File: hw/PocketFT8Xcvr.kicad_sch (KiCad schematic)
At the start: 55 parts, among them J1 HX8357D, J2 ANT, J3 +12V, J4 Conn_01x07, Q1 2N3904, Q2 2N3906, Q3 2N7000, Q4 2N7000, U1 MCP3422, U2 Si4735-D60-GU, U3 GVA-84, U4 L7805CV

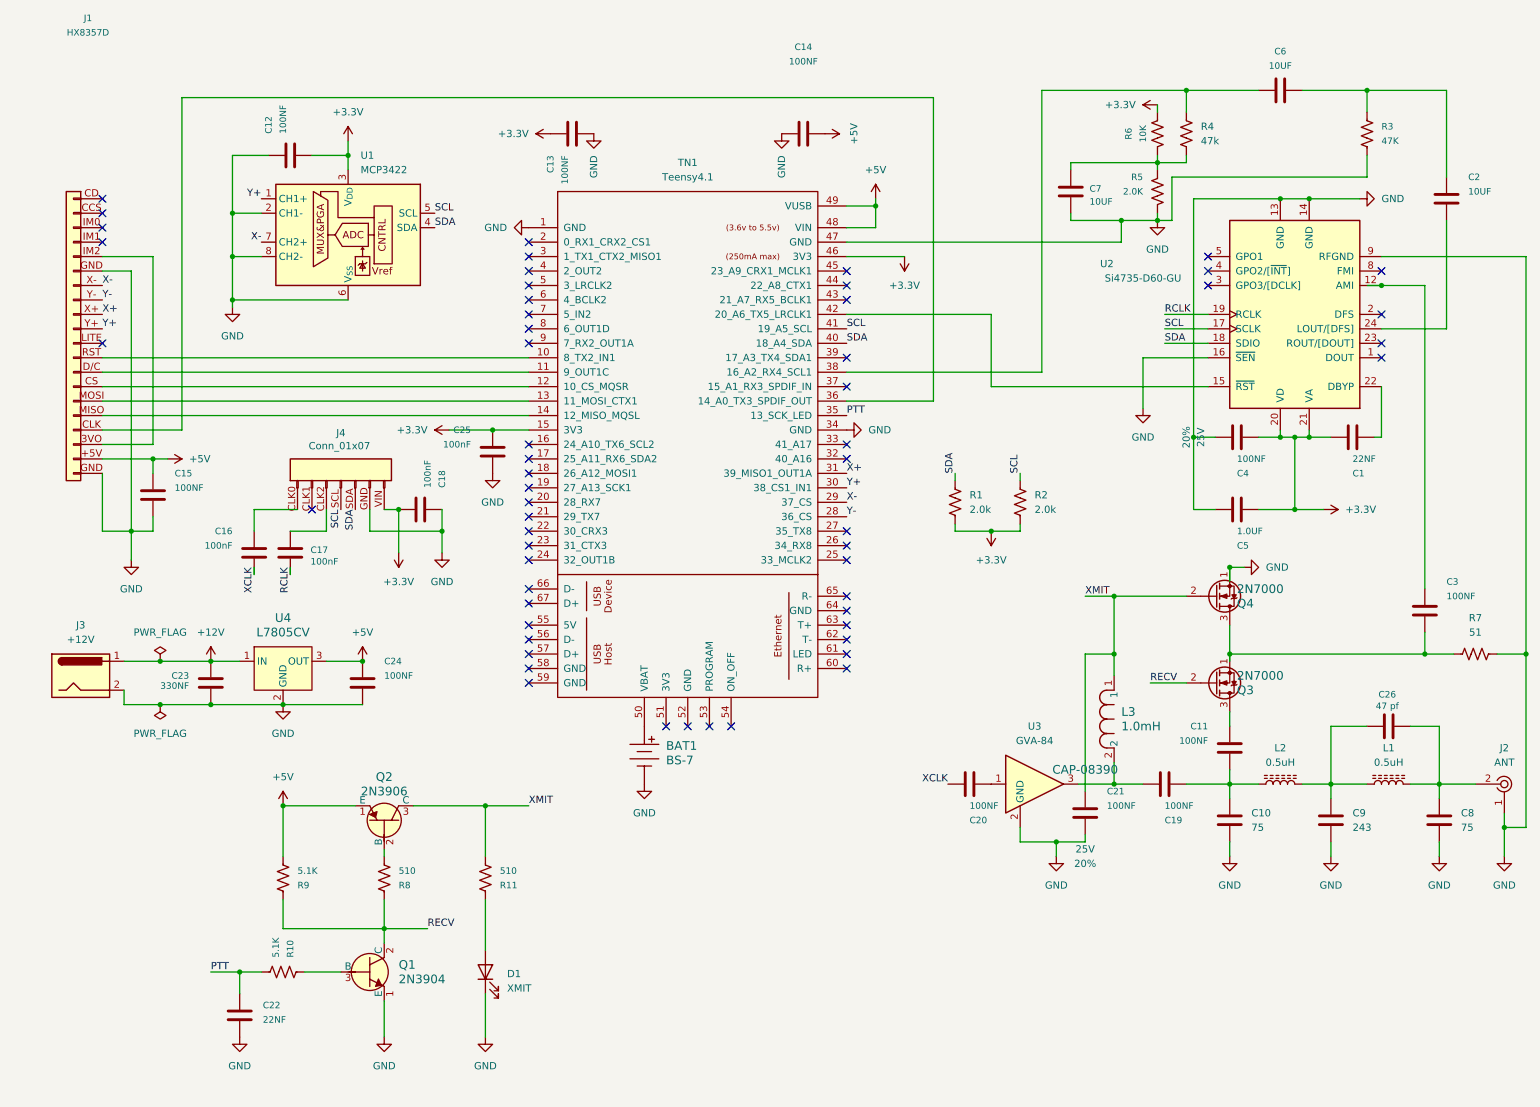
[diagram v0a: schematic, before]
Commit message: BOM construction begun
Connectors and capacitors
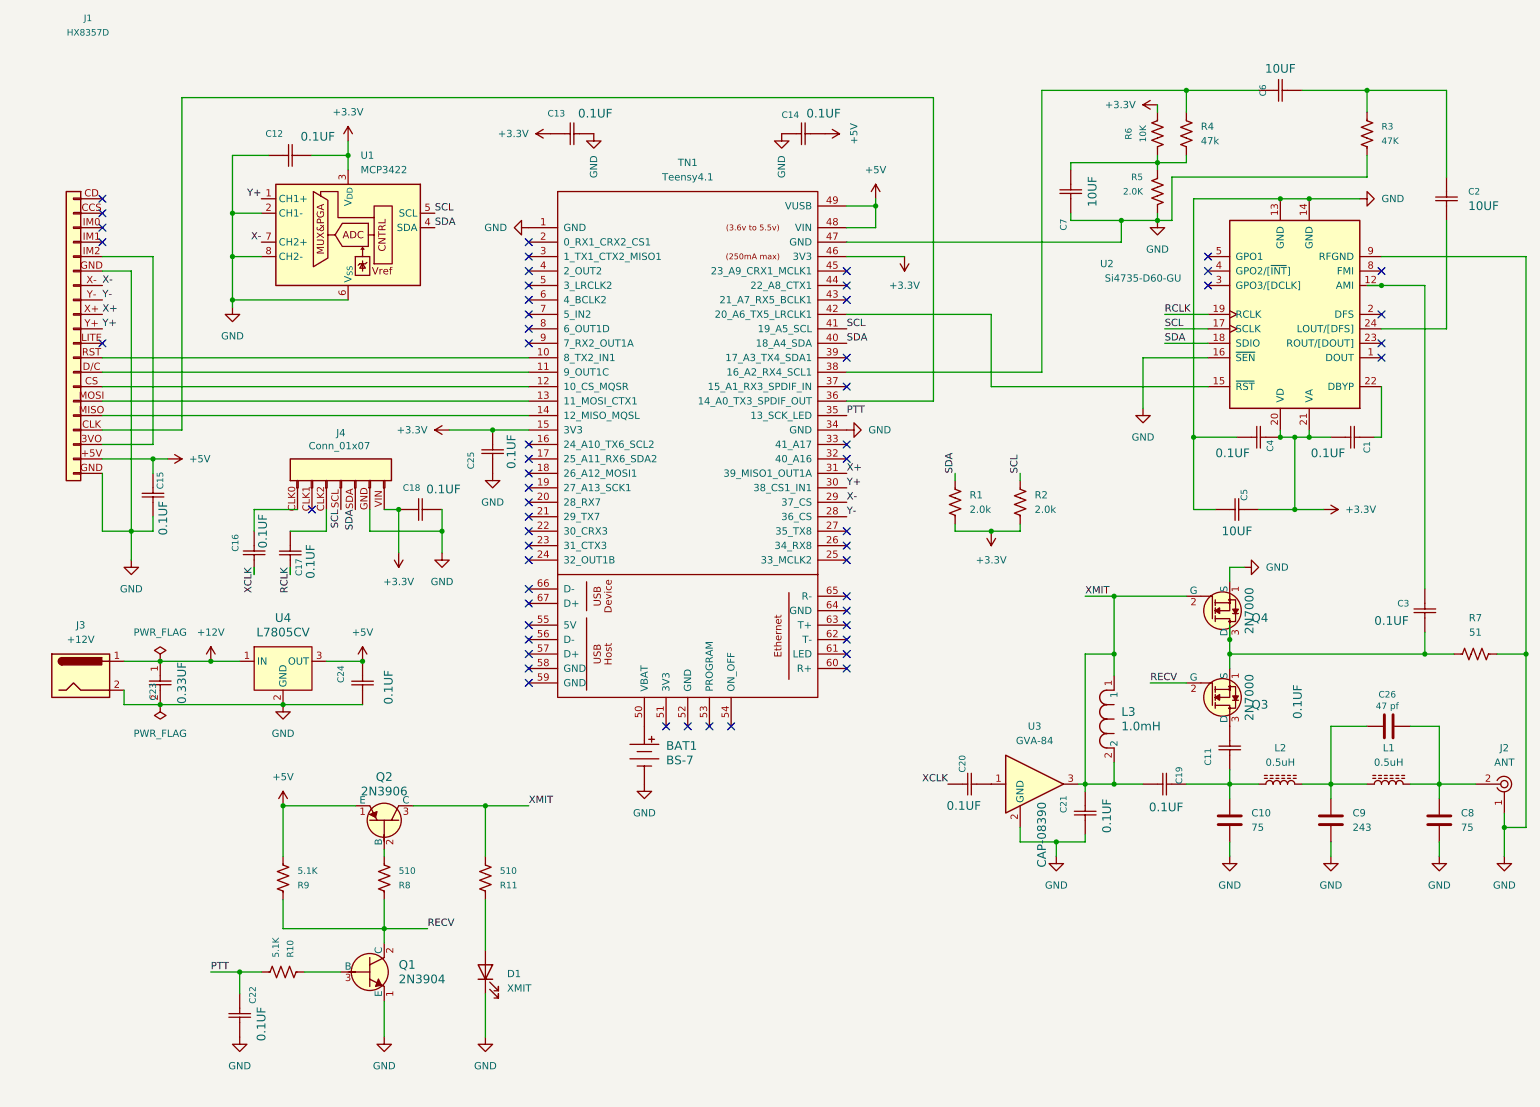
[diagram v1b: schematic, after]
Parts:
- C1, C22: value 22NF -> 0.1UF; footprint SparkFun-Capacitor:C_0603_1608Metric -> 0603; symbol SparkFun-Capacitor:0.1uF_0603_25V_20% -> Kemet2024-08-02_22-05-35:C0603C104K4RACTU; Manufacturer (none) -> Kemet; Mfg Part # (none) -> C0603C104K4RAC7867; Tolerance 20% -> 10%; Voltage 25V -> 16V
- C11, C12, C13, C14, C15, C19, C20, C21, C24, C3, C4: value 100NF -> 0.1UF; footprint SparkFun-Capacitor:C_0603_1608Metric -> 0603; symbol SparkFun-Capacitor:0.1uF_0603_25V_20% -> Kemet2024-08-02_22-05-35:C0603C104K4RACTU; Manufacturer (none) -> Kemet; Mfg Part # (none) -> C0603C104K4RAC7867; Tolerance 20% -> 10%; Voltage 25V -> 16V
- C16, C17, C18, C25: value 100nF -> 0.1UF; footprint SparkFun-Capacitor:C_0603_1608Metric -> 0603; symbol SparkFun-Capacitor:0.1uF_0603_25V_20% -> Kemet2024-08-02_22-05-35:C0603C104K4RACTU; Manufacturer (none) -> Kemet; Mfg Part # (none) -> C0603C104K4RAC7867; Tolerance 20% -> 10%; Voltage 25V -> 16V
- C2, C6, C7: footprint SparkFun-Capacitor:C_0603_1608Metric -> 0805; symbol SparkFun-Capacitor:10uF_0603_6.3V_20% -> Kemet2024-08-02_22-55-33:C0805C334K4RAC7800; Manufacturer (none) -> Kemet; Mfg Part # (none) -> C0805C106K4PAC7800
- C23: value 330NF -> 0.33UF; footprint 0603 -> 0805; symbol Device:C -> Kemet2024-08-02_22-55-33:C0805C334K4RAC7800; Manufacturer (none) -> Kemet; Mfg Part # (none) -> C0805C334K4RAC7800
- C5: value 1.0UF -> 10UF; footprint SparkFun-Capacitor:C_0603_1608Metric -> 0805; symbol SparkFun-Capacitor:1.0uF_0603_16V_10% -> Kemet2024-08-02_22-55-33:C0805C334K4RAC7800; Manufacturer (none) -> Kemet; Mfg Part # (none) -> C0805C106K4PAC7800
- Q3, Q4: footprint Package_TO_SOT_THT:TO-92_Inline -> digikey-footprints:TO-92-3; symbol Transistor_FET:2N7000 -> dk_Transistors-FETs-MOSFETs-Single:2N7000; Category (none) -> Discrete Semiconductor Products; DK_Datasheet_Link (none) -> https://www.onsemi.com/pub/Collateral/NDS7002A-D.PDF; DK_Detail_Page (none) -> /product-detail/en/on-semiconductor/2N7000/2N7000FS-ND/2442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; Description_1 (none) -> MOSFET N-CH 60V 200MA TO-92; Digi-Key_PN (none) -> 2N7000FS-ND; Family (none) -> Transistors - FETs, MOSFETs - Single; MPN (none) -> 2N7000; Manufacturer (none) -> ON Semiconductor; Status (none) -> Active
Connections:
- net +3.3V: now also C1.1, C12.1, C4.2, C5.2; no longer C1.2, C12.2, C4.1, C5.1
- net +5V: now also C14.2, C15.2, C24.2; no longer C14.1, C15.1, C24.1
- net GND: now also C12.2, C14.1, C15.1, C21.1, C22.1, C24.1, C4.1, C5.1, C7.1; no longer C12.1, C14.2, C15.2, C21.2, C22.2, C24.2, C4.2, C5.2, C7.2
- net PTT: now also C22.2; no longer C22.1
- net RCLK: now also C17.1; no longer C17.2
- net XCLK: now also C20.1; no longer C20.2
- net XMIT: now also C19.1, C21.2, L3.2, U3.3; no longer C21.1
- net at R4.1, R5.2, R6.1: now also C7.2; no longer C7.1
- net at Q3.1 (S), Q4.3 (D), R7.2: now also C3.1; no longer C3.2
- net at C10.1, C11.2, L2.1: now also C19.2; no longer C19.1
- net at U2.22 (DBYP): now also C1.2; no longer C1.1
- net at R4.2, TN1.38 (16_A2_RX4_SCL1): now also C6.2; no longer C6.1
- net at C2.2: now also C6.1, R3.2; no longer U2.24 (LOUT/[DFS])
- net at U3.1: now also C20.2; no longer C20.1
- net at U2.12 (AMI): now also C3.2; no longer C3.1
- net at J4.CLK2: now also C17.2; no longer C17.1
- new net: C2.1, U2.24 (LOUT/[DFS])

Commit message: Ongoing construction of BOM
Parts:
- removed R8: 510, SparkFun-Resistor:R_0603_1608Metric, symbol SparkFun-Resistor:2.0k_0603
- added R8: 510, 0603, symbol Device:R_US
- C1, C11, C12, C13, C14, C15, C16, C17, C18, C19, C2, C20, C21, C22, C23, C24, C25, C3, C4, C5, C6, C7: Notes (none) -> Substitutions OK
- C10, C8: value 75 -> 75PF; now not fitted; now left out of the parts list
- C26: value 47 pf -> 47PF; footprint Capacitor_SMD:C_0805_2012Metric -> 0805; now not fitted; now left out of the parts list
- C9: value 243 -> 243PF; now not fitted; now left out of the parts list
- L1, L2: now not fitted; now left out of the parts list
- L3: Manufacturer (none) -> Bourns; Mfg Part # (none) -> RLB9012-102KL
- Q3: Mfg Part # (none) -> 2N7000
- Q4: Mfg Part # (none) -> 2N7000; Notes (none) -> Substitions OK; Status Active -> (none)
- R1: value 2.0k -> 2.0K; footprint SparkFun-Resistor:R_0603_1608Metric -> 0603; Manufacturer (none) -> Yageo; Mfg Part # (none) -> RC0603JR-072KL; Notes (none) -> Substitutions OK; PROD_ID RES-08296 -> (none)
- R10, R9: footprint SparkFun-Resistor:R_0603_1608Metric -> 0603; Manufacturer (none) -> Yageo; Mfg Part # (none) -> RC0603JR-075K1L; Notes (none) -> Substitutions OK; PROD_ID RES-12083 -> (none)
- R11: footprint SparkFun-Resistor:R_0603_1608Metric -> 0603; symbol SparkFun-Resistor:2.0k_0603 -> Device:R_US; Manufacturer (none) -> Yageo; Mfg Part # (none) -> RC0603JR-07510RL; Notes (none) -> Substitutions OK
- R2: footprint SparkFun-Resistor:R_0603_1608Metric -> 0603; Manufacturer (none) -> Yageo; Mfg Part # (none) -> RC0603JR-072KL; Notes (none) -> Substitutions OK
- R3, R4: footprint SparkFun-Resistor:R_0603_1608Metric -> 0603; Manufacturer (none) -> Yageo; Mfg Part # (none) -> RC0603JR-0747KL; Notes (none) -> Substitutions OK
- R6: footprint SparkFun-Resistor:R_0603_1608Metric -> 0603; Manufacturer (none) -> YAGEO; Mfg Part # (none) -> RC0603JR-0710KL; Notes (none) -> Substitutions OK
- R7: value 51 -> 51 OHM
- U4: MPN L7805CV -> (none); Mfg Part # (none) -> L7805CV
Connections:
- net RECV: now also R8.2
- net XMIT: now also R11.1; no longer R11.2
- net at Q2.2 (B): now also R8.1
- net at D1.2 (A): now also R11.2; no longer R11.1
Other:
- moved on the sheet: R11, R9

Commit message: Ongoing BOM construction
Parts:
- BAT1: MPN BS-7 -> (none); Mfg Part # (none) -> BS-7; Type (none) -> SMD
- C1, C11, C12, C13, C14, C15, C16, C17, C18, C19, C2, C20, C21, C22, C23, C24, C25, C3, C4, C5, C6, C7, R1, R10, R3, R6, R9: Type (none) -> SMD
- D1, J1, J4, TN1: now not fitted; now left out of the parts list
- J2: Mfg Part # (none) -> 5-1814400-1; Notes (none) -> Substitutions OK; Type (none) -> SMD
- J3: footprint (none) -> CONN1x2_PJ-037A_CUD; symbol Connector:Barrel_Jack -> BarrelJackTHT:PJ-037A; Manufacturer (none) -> CUI Devices; Mfg Part # (none) -> PJ-037A; Type (none) -> THT; now not fitted; now left out of the parts list
- L3: Type (none) -> SMD; now not fitted; now left out of the parts list
- Q1: MPN 2N3904 -> (none); Mfg Part # (none) -> 2N3904; Type (none) -> THT; now not fitted; now left out of the parts list
- Q2: MPN 2N3906 -> (none); Mfg Part # (none) -> 2N3906; Type (none) -> THT; now not fitted; now left out of the parts list
- Q3, Q4: Type (none) -> THT; now not fitted; now left out of the parts list
- R11, R8: value 510 -> 510 Ohm; Type (none) -> SMD
- R2: value 2.0k -> 2.0K; Type (none) -> SMD
- R4: value 47k -> 47K; Type (none) -> SMD
- R5: footprint SparkFun-Resistor:R_0603_1608Metric -> 0603; Manufacturer (none) -> Yageo; Mfg Part # (none) -> RC0603JR-072KL; Notes (none) -> Substitutions OK; Type (none) -> SMD
- R7: Manufacturer (none) -> Yageo; Mfg Part # (none) -> RC1210JR-0751RL; Notes (none) -> Substitutions OK; Type (none) -> SMD
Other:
- moved on the sheet: C4

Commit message: BOM Complete
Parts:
- U1: value MCP3422 -> MCP3422A1T-E/SN; Manufacturer (none) -> Microchip Technology; Mfg Part # (none) -> MCP3422A1T-E/SN; Type (none) -> SMD
- U2: Manufacturer (none) -> Skyworks Solutions; Mfg Part # (none) -> SI4735-D60-GU; Type (none) -> SMD
- U3: value GVA-84 -> GVA-84+; footprint Package_TO_SOT_SMD:SOT-89-3 -> SOT-89-4; Manufacturer (none) -> Mini-Circuits; Mfg Part # (none) -> GVA-84+; Type (none) -> SMD
- U4: footprint digikey-footprints:TO-220-3 -> TO-220-3; Type (none) -> SMD
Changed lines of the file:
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@@
+	)
+	(symbol
+		(lib_id "power:GND")
+		(at 193.04 137.16 180)
+		(unit 1)
+		(exclude_from_sim no)
+		(in_bom yes)
+		(on_board yes)
+		(dnp no)
+		(fields_autoplaced yes)
+		(property "Reference" "#PWR037"
+			(at 193.04 130.81 0)
+			(effects
+				(font
+					(size 1.27 1.27)
+				)
+				(hide yes)
+			)
+		)
+		(property "Value" "GND"
+			(at 193.04 132.08 0)
+			(effects
+				(font
+					(size 1.27 1.27)
+				)
+			)
+		)
+		(property "Footprint" ""
+			(at 193.04 137.16 0)
+			(effects
+				(font
+					(size 1.27 1.27)
+				)
+				(hide yes)
+			)
+		)
+		(property "Datasheet" ""
+			(at 193.04 137.16 0)
+			(effects
+				(font
+					(size 1.27 1.27)
+				)
+				(hide yes)
+			)
+		)
+		(property "Description" "Power symbol creates a global label with name \"GND\" , ground"
+			(at 193.04 137.16 0)
+			(effects
+				(font
+					(size 1.27 1.27)
+				)
+				(hide yes)
+			)
+		)
+		(pin "1"
+		)
+		(instances
+			(project ""
+				(path "/9b703ee0-e32d-4836-8d5c-bb1a7416ca3c"
+					(reference "#PWR037")
+					(unit 1)
+				)
+			)
+		)
 	)
 	(symbol
@@
 			)
 		)
-		(property "Footprint" "digikey-footprints:TO-220-3"
+		(property "Footprint" "TO-220-3"
 			(at 66.04 115.57 0)
 			(effects
@@
 				)
 				(justify left)
+				(hide yes)
+			)
+		)
+		(property "Type" "SMD"
+			(at 60.96 120.65 0)
+			(effects
+				(font
+					(size 1.27 1.27)
+				)
 				(hide yes)
 			)
@@
 			)
 		)
-		(property "Value" "MCP3422"
+		(property "Value" "MCP3422A1T-E/SN"
 			(at 74.5841 34.29 0)
 			(effects
@@
 			)
 		)
-		(property "Description" "2-Channel, 18-Bit, Delta-Sigma AD-Converter, I²C Interface, Reference, SOIC-8"
+		(property "Description" "IC ADC 18BIT SIGMA-DELTA 8SOIC"
+			(at 72.39 44.45 0)
+			(effects
+				(font
+					(size 1.27 1.27)
+				)
+				(justify bottom)
+				(hide yes)
+			)
+		)
+		(property "Mfg Part #" "MCP3422A1T-E/SN"
+			(at 72.39 44.45 0)
+			(effects
+				(font
+					(size 1.27 1.27)
+				)
+				(hide yes)
+			)
+		)
+		(property "Notes" ""
+			(at 72.39 44.45 0)
+			(effects
+				(font
+					(size 1.27 1.27)
+				)
+				(hide yes)
+			)
+		)
+		(property "Type" "SMD"
+			(at 72.39 44.45 0)
+			(effects
+				(font
+					(size 1.27 1.27)
+				)
+				(hide yes)
+			)
+		)
+		(property "Manufacturer" "Microchip Technology"
 			(at 72.39 44.45 0)
 			(effects
@@
 		(on_board yes)
 		(dnp no)
-		(fields_autoplaced yes)
 		(property "Reference" "U3"
-			(at 193.04 132.08 0)
-			(effects
-				(font
-					(size 1.27 1.27)
-				)
-			)
-		)
-		(property "Value" "GVA-84"
-			(at 193.04 134.62 0)
-			(effects
-				(font
-					(size 1.27 1.27)
-				)
-			)
-		)
-		(property "Footprint" "Package_TO_SOT_SMD:SOT-89-3"
+			(at 188.976 135.89 0)
+			(effects
+				(font
+					(size 1.27 1.27)
+				)
+			)
+		)
+		(property "Value" "GVA-84+"
+			(at 198.12 137.922 0)
+			(effects
+				(font
+					(size 1.27 1.27)
+				)
+			)
+		)
+		(property "Footprint" "SOT-89-4"
 			(at 194.31 132.08 0)
 			(effects
@@
 			)
 		)
+		(property "Manufacturer" "Mini-Circuits"
+			(at 193.04 142.24 0)
+			(effects
+				(font
+					(size 1.27 1.27)
+				)
+				(hide yes)
+			)
+		)
+		(property "Mfg Part #" "GVA-84+"
+			(at 193.04 142.24 0)
+			(effects
+				(font
+					(size 1.27 1.27)
+				)
+				(hide yes)
+			)
+		)
+		(property "Type" "SMD"
+			(at 193.04 142.24 0)
+			(effects
+				(font
+					(size 1.27 1.27)
+				)
+				(hide yes)
+			)
+		)
+		(property "Notes" ""
+			(at 193.04 142.24 0)
+			(effects
+				(font
+					(size 1.27 1.27)
+				)
+				(hide yes)
+			)
+		)
 		(pin "1"
 		)
@@
 		)
 		(pin "3"
+		)
+		(pin "4"
 		)
 		(instances
@@
 			)
 		)
-		(property "Description" "AM/FM/SW/LW Broadcast Radio Receiver with RDS/RBDS"
+		(property "Description" "RF RX AM/FM 153KHZ-279KHZ 24SSOP"
 			(at 238.76 59.69 0)
 			(effects
+				(font
+					(size 1.27 1.27)
+				)
+				(hide yes)
+			)
+		)
+		(property "Manufacturer" "Skyworks Solutions"
+			(at 238.76 59.69 0)
+			(effects
+				(font
+					(size 1.27 1.27)
+				)
+				(hide yes)
+			)
+		)
+		(property "Mfg Part #" "SI4735-D60-GU"
+			(at 238.76 59.69 0)
+			(effects
+				(font
+					(size 1.27 1.27)
+				)
+				(hide yes)
+			)
+		)
+		(property "Notes" ""
+			(at 238.76 59.69 0)
+			(effects
+				(font
+					(size 1.27 1.27)
+				)
+				(hide yes)
+			)
+		)
+		(property "Type" "SMD"
+			(at 238.76 59.69 0)
+			(effects
